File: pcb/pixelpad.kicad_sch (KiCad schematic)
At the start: 16 parts, among them SW1 SW_Push_45deg, SW2 SW_Push_45deg, SW3 SW_Push_45deg, SW4 SW_Push_45deg, SW5 SW_Push_45deg, SW6 RotaryEncoder_Switch, U1 MOUDLE-SEEEDUINO-XIAO, U2 ER_OLEDM0.91_1x-I2C

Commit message: Reordered
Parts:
- removed SW3: SW_Push_45deg, Button_Switch_Keyboard:SW_Cherry_MX_1.00u_PCB, symbol KiCad-User:SW_Push_45deg
- added SW6: SW_Push_45deg, Button_Switch_Keyboard:SW_Cherry_MX_1.00u_PCB, symbol KiCad-User:SW_Push_45deg
- renumbered SW6 to SW3
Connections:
- net COL0: now also SW4.1, U1.1 (PA02_A0_D0); no longer U1.2 (PA4_A1_D1)
- net COL1: now also SW5.1, U1.11 (PA6_A10_D10_MOSI); no longer SW4.1, U1.1 (PA02_A0_D0)
- net COL2: now also SW6.1; no longer SW5.1
- net at D6.2 (A): now also SW4.2
- net at D7.2 (A): now also SW5.2; no longer SW4.2
- net at D8.2 (A): now also SW6.2; no longer SW5.2
- no-connect marks 0 -> 3
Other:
- moved on the sheet: D1, D2

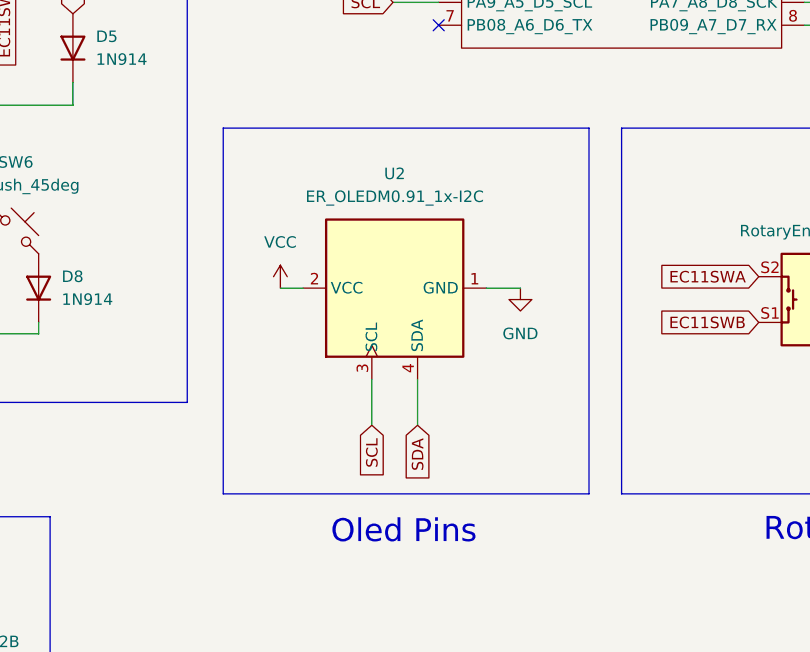
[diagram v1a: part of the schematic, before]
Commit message: Added 4pin connector instead of the actual footprint
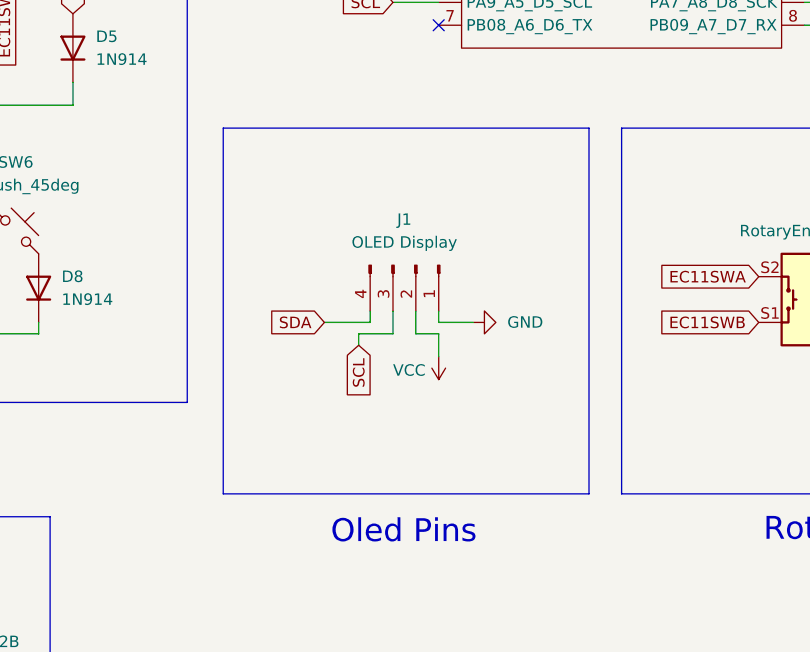
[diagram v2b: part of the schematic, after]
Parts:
- removed U2: ER_OLEDM0.91_1x-I2C, Display:ER_OLEDM0.91_1x-I2C, symbol KiCad-User:ER_OLEDM0.91_1x-I2C
- added J1: OLED Display, Connector_PinHeader_2.54mm:PinHeader_1x04_P2.54mm_Vertical, symbol Connector:Conn_01x04_Pin
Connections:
- net GND: now also J1.1 (Pin_1)
- net SCL: now also J1.3 (Pin_3)
- net SDA: now also J1.4 (Pin_4)
- net VCC: now also J1.2 (Pin_2)

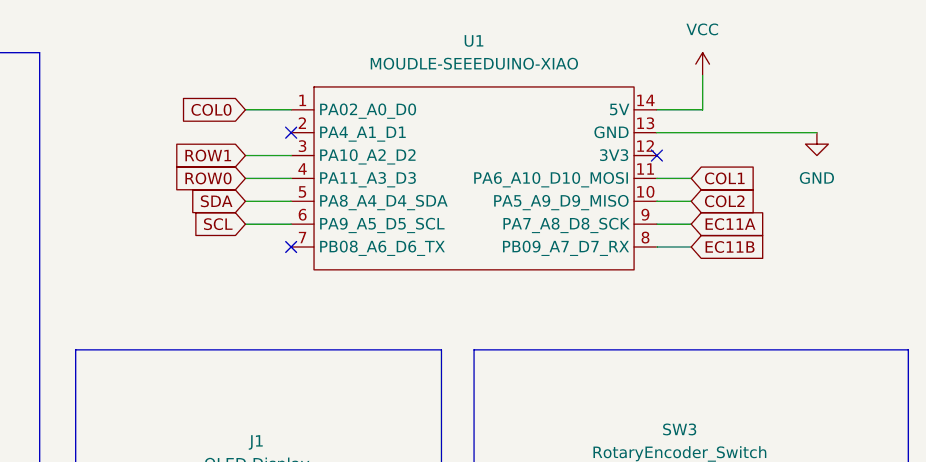
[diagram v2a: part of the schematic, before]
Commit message: Reordering pins so it's easier to route
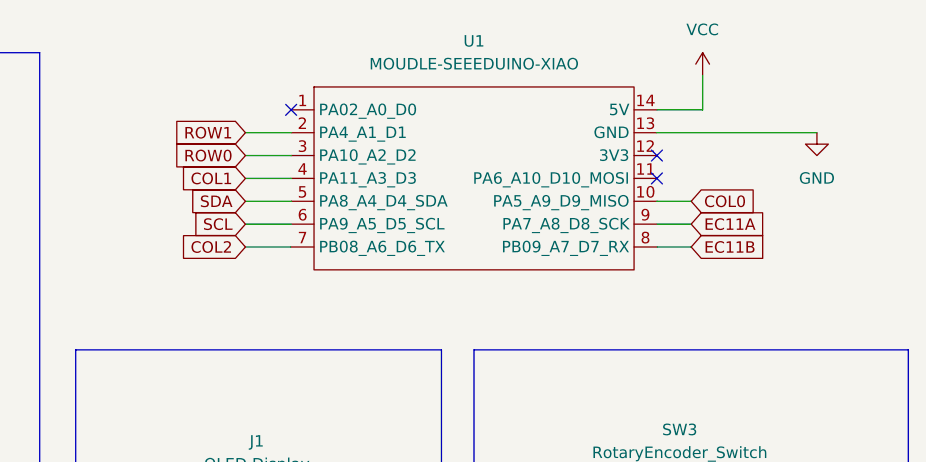
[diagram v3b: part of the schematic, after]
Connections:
- net COL0: now also U1.10 (PA5_A9_D9_MISO); no longer U1.1 (PA02_A0_D0)
- net COL1: now also U1.4 (PA11_A3_D3); no longer U1.11 (PA6_A10_D10_MOSI)
- net COL2: now also U1.7 (PB08_A6_D6_TX); no longer U1.10 (PA5_A9_D9_MISO)
- net ROW0: now also U1.3 (PA10_A2_D2); no longer U1.4 (PA11_A3_D3)
- net ROW1: now also U1.2 (PA4_A1_D1); no longer U1.3 (PA10_A2_D2)

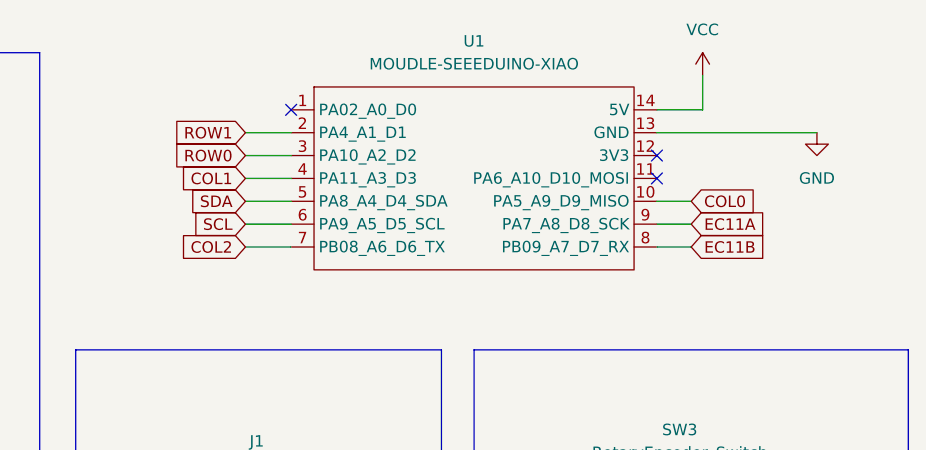
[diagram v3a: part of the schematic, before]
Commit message: Ran DRC and no more errors
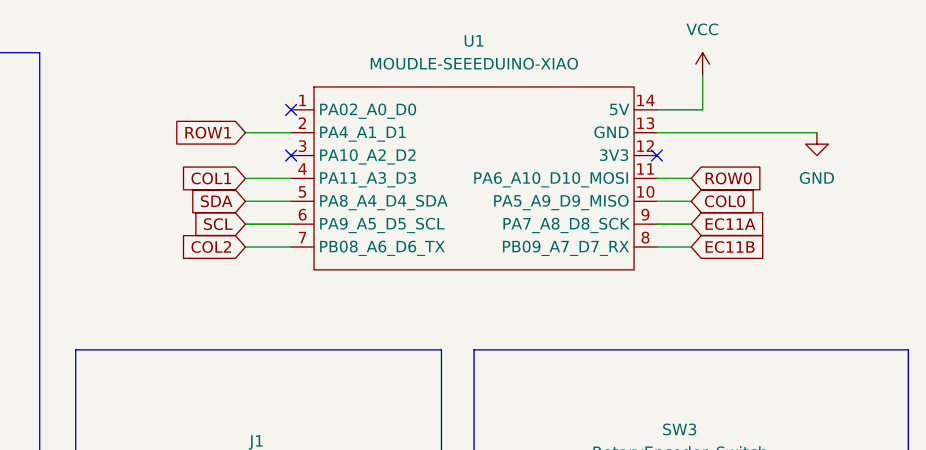
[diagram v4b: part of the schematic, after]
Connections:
- net ROW0: now also U1.11 (PA6_A10_D10_MOSI); no longer U1.3 (PA10_A2_D2)
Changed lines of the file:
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@@
 	)
 	(no_connect
-		(at 167.64 31.75)
+		(at 127 29.21)
 	)
 	(no_connect
@@
 	(wire
 		(pts
-			(xy 121.92 29.21) (xy 127 29.21)
-		)
-		(stroke
-			(width 0)
-			(type default)
-		)
-	)
-	(wire
-		(pts
 			(xy 41.91 73.66) (xy 41.91 72.39)
 		)
@@
 		(pts
 			(xy 114.3 72.39) (xy 119.38 72.39)
+		)
+		(stroke
+			(width 0)
+			(type default)
+		)
+	)
+	(wire
+		(pts
+			(xy 167.64 31.75) (xy 171.45 31.75)
 		)
 		(stroke
@@
 		)
 	)
+	(global_label "ROW0"
+		(shape input)
+		(at 171.45 31.75 0)
+		(fields_autoplaced yes)
+		(effects
+			(font
+				(size 1.27 1.27)
+			)
+			(justify left)
+		)
+		(property "Intersheetrefs" "${INTERSHEET_REFS}"
+			(at 179.6966 31.75 0)
+			(hide yes)
+			(show_name no)
+			(do_not_autoplace no)
+			(effects
+				(font
+					(size 1.27 1.27)
+				)
+				(justify left)
+			)
+		)
+		(property "Netclass" "Default"
+			(at 171.45 35.5918 0)
+			(hide yes)
+			(show_name no)
+			(do_not_autoplace no)
+			(effects
+				(font
+					(size 1.27 1.27)
+					(italic yes)
+				)
+				(justify left)
+			)
+		)
+	)
 	(global_label "EC11SWB"
 		(shape input)
@@
 			)
 		)
-	)
-	(global_label "ROW0"
-		(shape input)
-		(at 121.92 29.21 180)
-		(fields_autoplaced yes)
-		(effects
-			(font
-				(size 1.27 1.27)
-			)
-			(justify right)
-		)
-		(property "Intersheetrefs" "${INTERSHEET_REFS}"
-			(at 113.6734 29.21 0)
-			(hide yes)
-			(show_name no)
-			(do_not_autoplace no)
-			(effects
-				(font
-					(size 1.27 1.27)
-				)
-				(justify right)
-			)
-		)
-		(property "Netclass" "Default"
-			(at 121.92 33.0518 0)
-			(hide yes)
-			(show_name no)
-			(do_not_autoplace no)
-			(effects
-				(font
-					(size 1.27 1.27)
-					(italic yes)
-				)
-				(justify right)
-			)
-		)

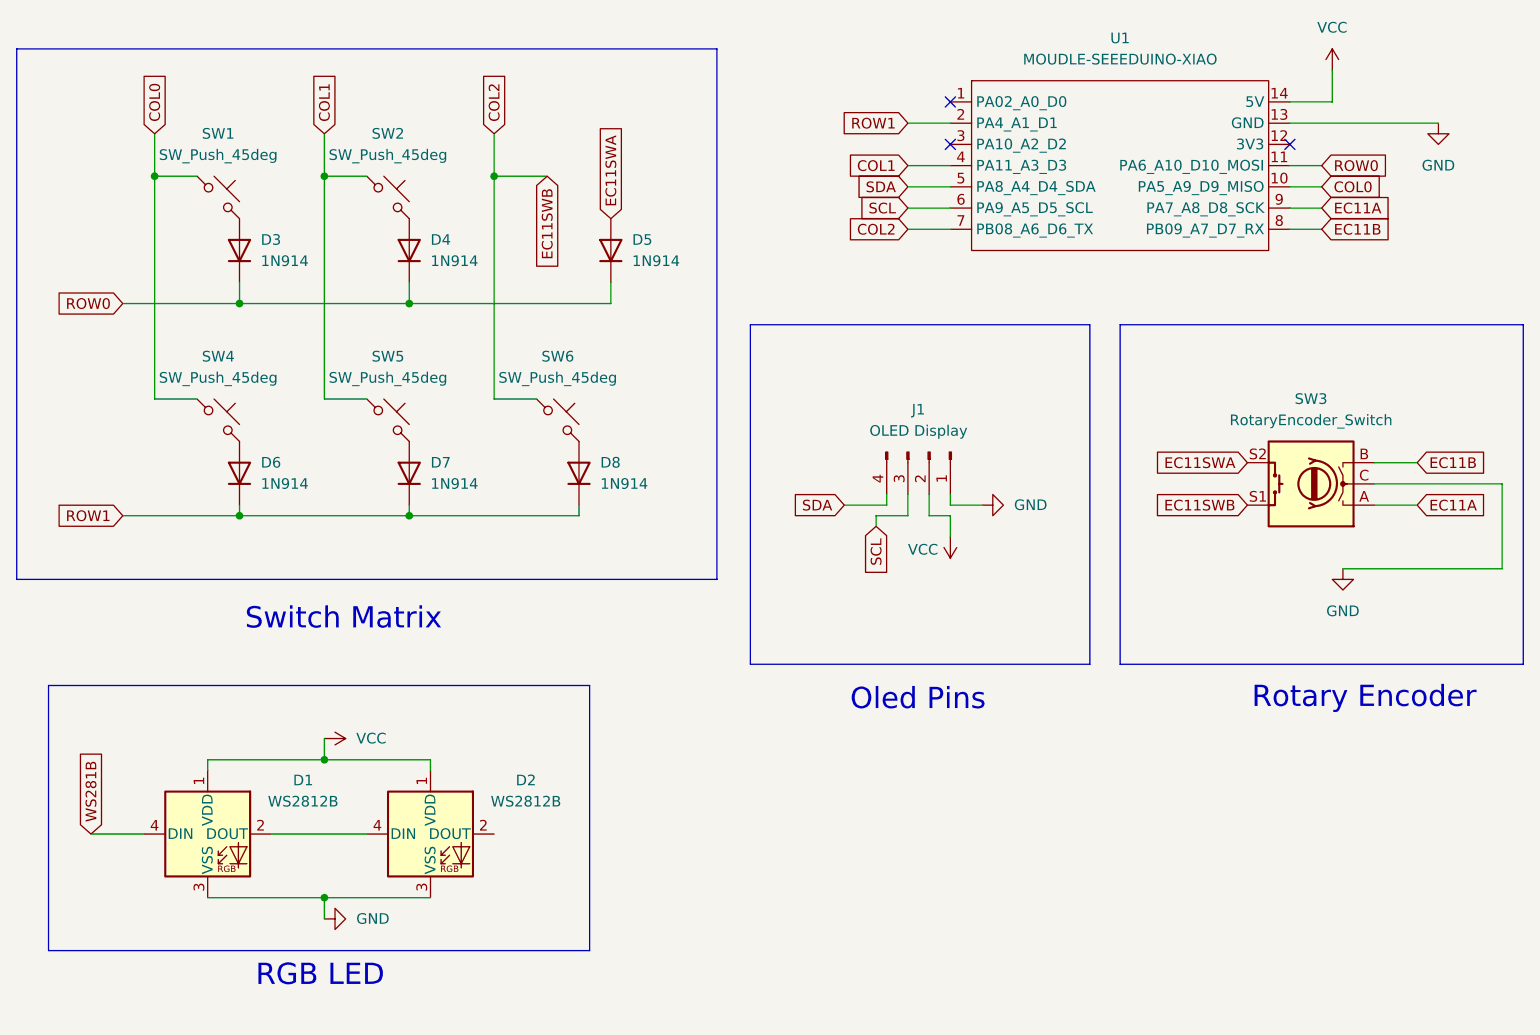
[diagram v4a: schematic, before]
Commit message: Fixed the led schematic and footprint to the right one
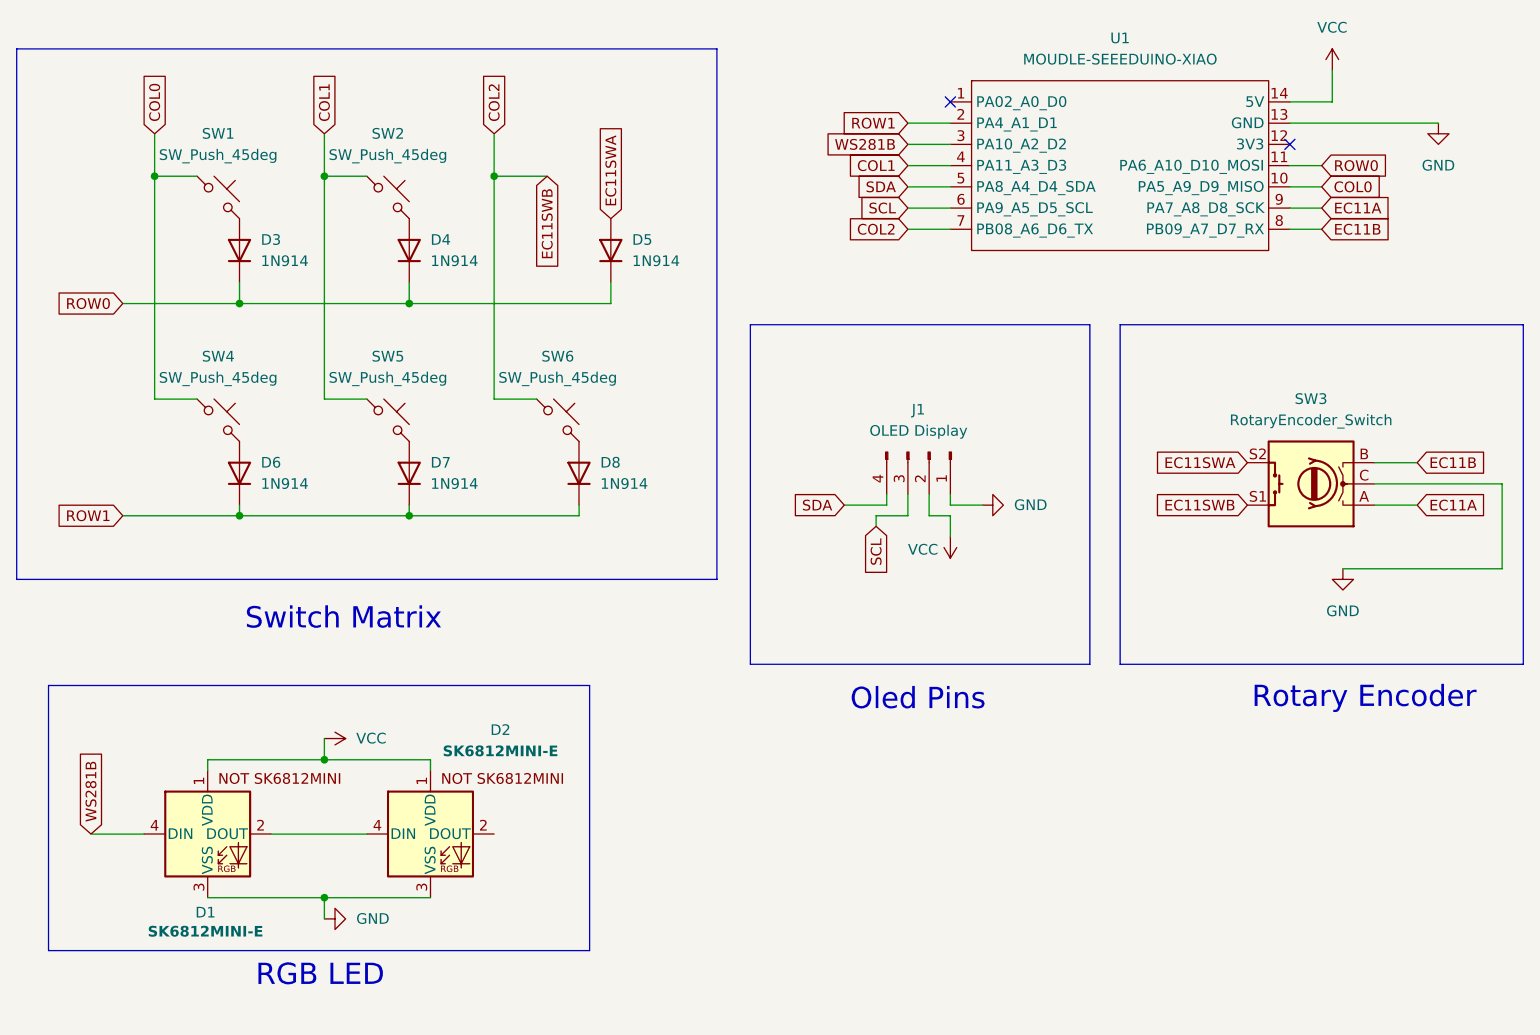
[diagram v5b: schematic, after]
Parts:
- removed D1, D2: WS2812B, LED_SMD:LED_WS2812B_PLCC4_5.0x5.0mm_P3.2mm, symbol KiCad-User:WS2812B
- added D1, D2: SK6812MINI-E, SK6812MINI-E - 3.2x2.8x1.78mm, symbol KiCad-User:SK6812MINI-E
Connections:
- net GND: now also D1.3 (VSS), D2.3 (VSS)
- net VCC: now also D1.1 (VDD), D2.1 (VDD)
- net WS281B: now also U1.3 (PA10_A2_D2), D1.4 (DIN)
- new net: D1.2 (DOUT), D2.4 (DIN)
- no-connect marks 3 -> 2
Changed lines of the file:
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@@
-	)
-	(no_connect
-		(at 127 29.21)
 	)
 	(no_connect
@@
 		(pts
 			(xy 62.23 45.72) (xy 62.23 48.26)
+		)
+		(stroke
+			(width 0)
+			(type default)
+		)
+	)
+	(wire
+		(pts
+			(xy 121.92 29.21) (xy 127 29.21)
 		)
 		(stroke
@@
 				)
 				(justify left)
+			)
+		)
+	)
+	(global_label "WS281B"
+		(shape input)
+		(at 121.92 29.21 180)
+		(fields_autoplaced yes)
+		(effects
+			(font
+				(size 1.27 1.27)
+			)
+			(justify right)
+		)
+		(property "Intersheetrefs" "${INTERSHEET_REFS}"
+			(at 111.3754 29.21 0)
+			(hide yes)
+			(show_name no)
+			(do_not_autoplace no)
+			(effects
+				(font
+					(size 1.27 1.27)
+				)
+				(justify right)
 			)
 		)
@@
 	)
 	(symbol
+		(lib_id "KiCad-User:SK6812MINI-E")
+		(at 38.1 111.76 0)
+		(unit 1)
+		(body_style 1)
+		(exclude_from_sim no)
+		(in_bom yes)
+		(on_board yes)
+		(in_pos_files yes)
+		(dnp no)
+		(property "Reference" "D1"
+			(at 37.846 121.158 0)
+			(show_name no)
+			(do_not_autoplace no)
+			(effects
+				(font
+					(size 1.27 1.27)
+				)
+			)
+		)
+		(property "Value" "SK6812MINI-E"
+			(at 37.846 123.444 0)
+			(show_name no)
+			(do_not_autoplace no)
+			(effects
+				(font
+					(size 1.27 1.27)
+					(thickness 0.254)
+					(bold yes)
+				)
+			)
+		)
+		(property "Footprint" "SK6812MINI-E - 3.2x2.8x1.78mm"
+			(at 39.37 119.38 0)
+			(hide yes)
+			(show_name no)
+			(do_not_autoplace no)
+			(effects
+				(font
+					(size 1.27 1.27)
+				)
+				(justify left top)
+			)
+		)
+		(property "Datasheet" "https://cdn-shop.adafruit.com/product-files/4960/4960_SK6812MINI-E_REV02_EN.pdf"
+			(at 40.64 121.285 0)
+			(hide yes)
+			(show_name no)
+			(do_not_autoplace no)
+			(effects
+				(font
+					(size 1.27 1.27)
+				)
+				(justify left top)
+			)
+		)
+		(property "Description" "RGB LED with integrated controller"
+			(at 38.1 111.76 0)
+			(hide yes)
+			(show_name no)
+			(do_not_autoplace no)
+			(effects
+				(font
+					(size 1.27 1.27)
+				)
+			)
+		)
+		(pin "4"
+		)
+		(pin "1"
+		)
+		(pin "2"
+		)
+		(pin "3"
+		)
+		(instances
+			(project "pixelpad"
+				(path "/3414973a-652a-4c78-88cc-120293b3a4e8"
+					(reference "D1")
+					(unit 1)
+				)
+			)
+		)
+	)
+	(symbol
 		(lib_id "KiCad-User:SW_Push_45deg")
 		(at 39.37 62.23 0)
@@
 				(path "/3414973a-652a-4c78-88cc-120293b3a4e8"
 					(reference "SW4")
-					(unit 1)
-				)
-			)
-		)
-	)
-	(symbol
-		(lib_id "KiCad-User:WS2812B")
-		(at 38.1 111.76 0)
-		(unit 1)
-		(body_style 1)
-		(exclude_from_sim no)
-		(in_bom yes)
-		(on_board yes)
-		(in_pos_files yes)
-		(dnp no)
-		(fields_autoplaced yes)
-		(property "Reference" "D1"
-			(at 49.53 105.3398 0)
-			(show_name no)
-			(do_not_autoplace no)
-			(effects
-				(font
-					(size 1.27 1.27)
-				)
-			)
-		)
-		(property "Value" "WS2812B"
-			(at 49.53 107.8798 0)
-			(show_name no)
-			(do_not_autoplace no)
-			(effects
-				(font
-					(size 1.27 1.27)
-				)
-			)
-		)
-		(property "Footprint" "LED_SMD:LED_WS2812B_PLCC4_5.0x5.0mm_P3.2mm"
-			(at 39.37 119.38 0)
-			(hide yes)
-			(show_name no)
-			(do_not_autoplace no)
-			(effects
-				(font
-					(size 1.27 1.27)
-				)
-				(justify left top)
-			)
-		)
-		(property "Datasheet" "https://cdn-shop.adafruit.com/datasheets/WS2812B.pdf"
-			(at 40.64 121.285 0)
-			(hide yes)
-			(show_name no)
-			(do_not_autoplace no)
-			(effects
-				(font
-					(size 1.27 1.27)
-				)
-				(justify left top)
-			)
-		)
-		(property "Description" "RGB LED with integrated controller"
-			(at 38.1 111.76 0)
-			(hide yes)
-			(show_name no)
-			(do_not_autoplace no)
-			(effects
-				(font
-					(size 1.27 1.27)
-				)
-			)
-		)
-		(pin "1"
-		)
-		(pin "3"
-		)
-		(pin "2"
-		)
-		(pin "4"
-		)
-		(instances
-			(project "pixelpad"
-				(path "/3414973a-652a-4c78-88cc-120293b3a4e8"
-					(reference "D1")
 					(unit 1)
 				)
@@
 	)
 	(symbol
-		(lib_id "KiCad-User:WS2812B")
+		(lib_id "KiCad-User:SK6812MINI-E")
 		(at 64.77 111.76 0)
 		(unit 1)
@@
 		(in_pos_files yes)
 		(dnp no)
-		(fields_autoplaced yes)
 		(property "Reference" "D2"
-			(at 76.2 105.3398 0)
-			(show_name no)
-			(do_not_autoplace no)
-			(effects
-				(font
-					(size 1.27 1.27)
-				)
-			)
-		)
-		(property "Value" "WS2812B"
-			(at 76.2 107.8798 0)
-			(show_name no)
-			(do_not_autoplace no)
-			(effects
-				(font
-					(size 1.27 1.27)
-				)
-			)
-		)
-		(property "Footprint" "LED_SMD:LED_WS2812B_PLCC4_5.0x5.0mm_P3.2mm"
+			(at 73.152 99.3139 0)
+			(show_name no)
+			(do_not_autoplace no)
+			(effects
+				(font
+					(size 1.27 1.27)
+				)
+			)
+		)
+		(property "Value" "SK6812MINI-E"
+			(at 73.152 101.854 0)
+			(show_name no)
+			(do_not_autoplace no)
+			(effects
+				(font
+					(size 1.27 1.27)
+					(thickness 0.254)
+					(bold yes)
+				)
+			)
+		)
+		(property "Footprint" "SK6812MINI-E - 3.2x2.8x1.78mm"
 			(at 66.04 119.38 0)
 			(hide yes)
@@
 			)
 		)
-		(property "Datasheet" "https://cdn-shop.adafruit.com/datasheets/WS2812B.pdf"
+		(property "Datasheet" "https://cdn-shop.adafruit.com/product-files/4960/4960_SK6812MINI-E_REV02_EN.pdf"
 			(at 67.31 121.285 0)
 			(hide yes)
@@
 			)
 		)
+		(pin "4"
+		)
 		(pin "1"
 		)
+		(pin "2"
+		)
 		(pin "3"
 		)
-		(pin "2"
-		)
-		(pin "4"
-		)
 		(instances
